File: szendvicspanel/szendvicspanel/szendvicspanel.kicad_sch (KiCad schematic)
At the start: 0 parts

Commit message: ANALOG_IN a mikrokontrolleres modulra is
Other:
- sheet Mikrovezérlő + PWM ports: added ANALOG_IN; removed none
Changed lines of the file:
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@@
+			)
+		)
+		(pin "ANALOG_IN" input
+			(at 121.92 156.21 180)
+			(effects
+				(font
+					(size 1.27 1.27)
+				)
+				(justify left)
 			)
 		)

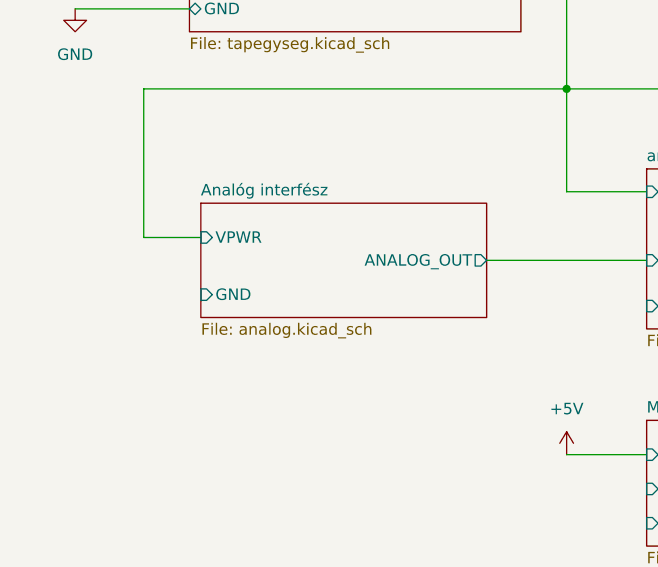
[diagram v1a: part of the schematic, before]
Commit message: KiCAD analóg interfész
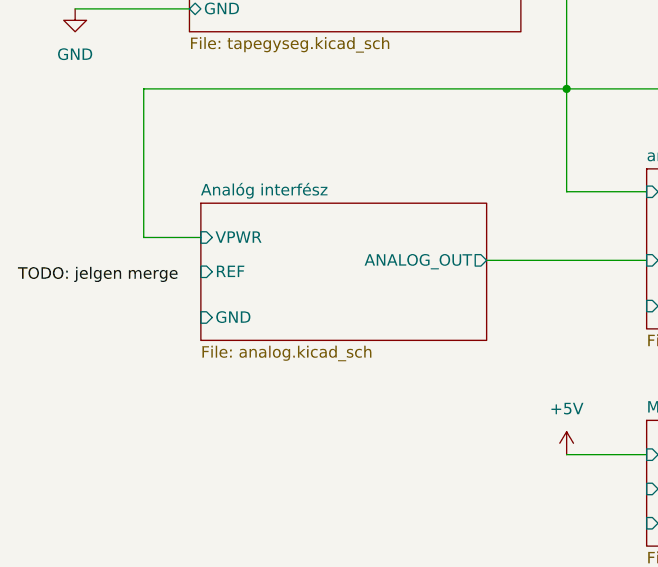
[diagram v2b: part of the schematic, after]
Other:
- sheet Analóg interfész ports: added REF; removed none
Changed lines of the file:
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@@
+		)
+	)
+	(label "TODO: jelgen merge"
+		(at 52.07 133.35 0)
+		(effects
+			(font
+				(size 1.27 1.27)
+			)
+			(justify left bottom)
 		)
 	)
@@
 	(sheet
 		(at 72.39 124.46)
-		(size 31.75 12.7)
+		(size 31.75 15.24)
 		(exclude_from_sim no)
 		(in_bom yes)
@@
 		)
 		(property "Sheetfile" "analog.kicad_sch"
-			(at 72.39 137.7446 0)
+			(at 72.39 140.2846 0)
 			(effects
 				(font
@@
 		)
 		(pin "GND" input
-			(at 72.39 134.62 180)
+			(at 72.39 137.16 180)
 			(effects
 				(font
@@
 			(effects
 				(font
+					(size 1.27 1.27)
+				)
+				(justify left)
+			)
+		)
+		(pin "REF" input
+			(at 72.39 132.08 180)
+			(effects
+				(font

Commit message: Analóg jelgen schematic copy+paste, output busz, analóg interfész pinjeinek frissítése
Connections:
- no-connect marks 0 -> 2
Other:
- sheet Analóg interfész ports: added +5V_IN, +5V_OUT, GND_IN, GND_OUT, REF_IN, VPWR_IN, VPWR_OUT, X; removed GND, REF, VPWR
- sheet analóg jelgen + PWM ports: added +5V, GND_IN, OUT{VPWR[1..8] GND[1..8] PWM[1..8]}, VPWR_IN; removed GND, PWM, SQR, TRI, VPWR
- note added: "Maximum 8 darab H-híd lehet"
- note removed: "TODO: 8 féle PWM 8 külön H-hídnak"

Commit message: Dokumentáció, Bandpass WIP
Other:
- sheet Analóg interfész ports: added none; removed REF_IN
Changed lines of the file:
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@@
-			)
-		)
-		(pin "REF_IN" input
-			(at 87.63 138.43 270)
-			(effects
-				(font
-					(size 1.27 1.27)
-				)
-				(justify left)
 			)
 		)

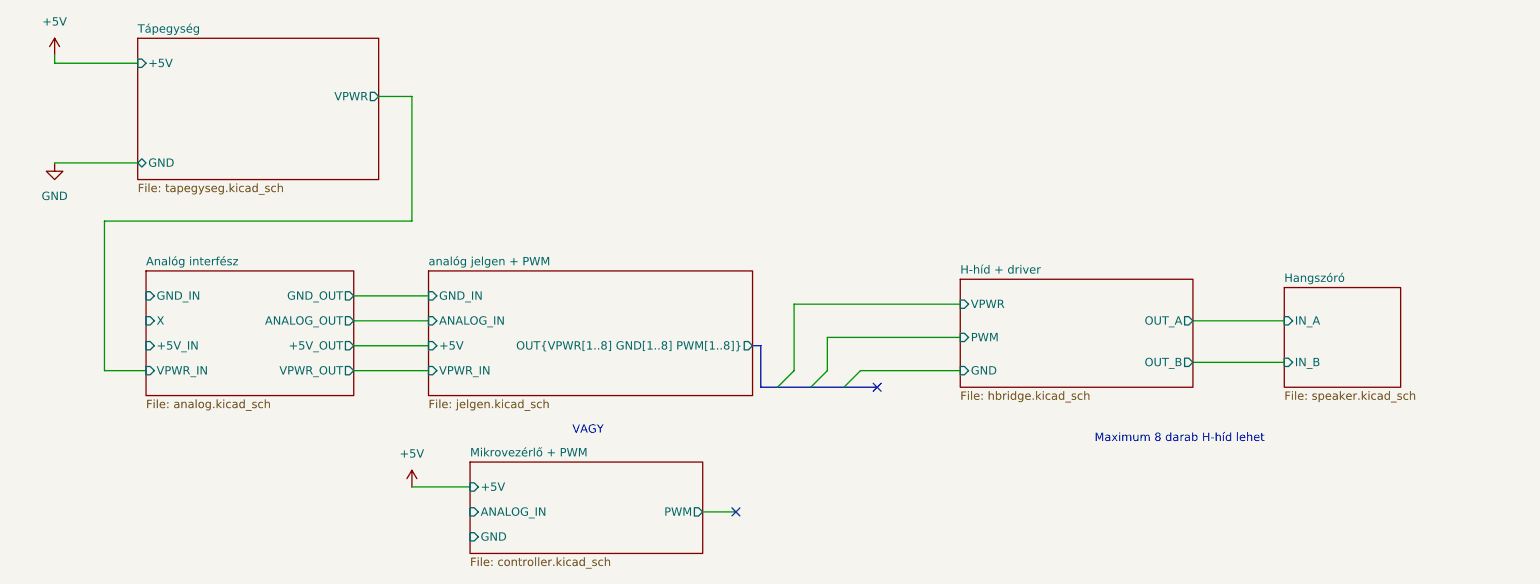
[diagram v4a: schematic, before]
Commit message: Átstrukturálás hierarchikus PCB-hez
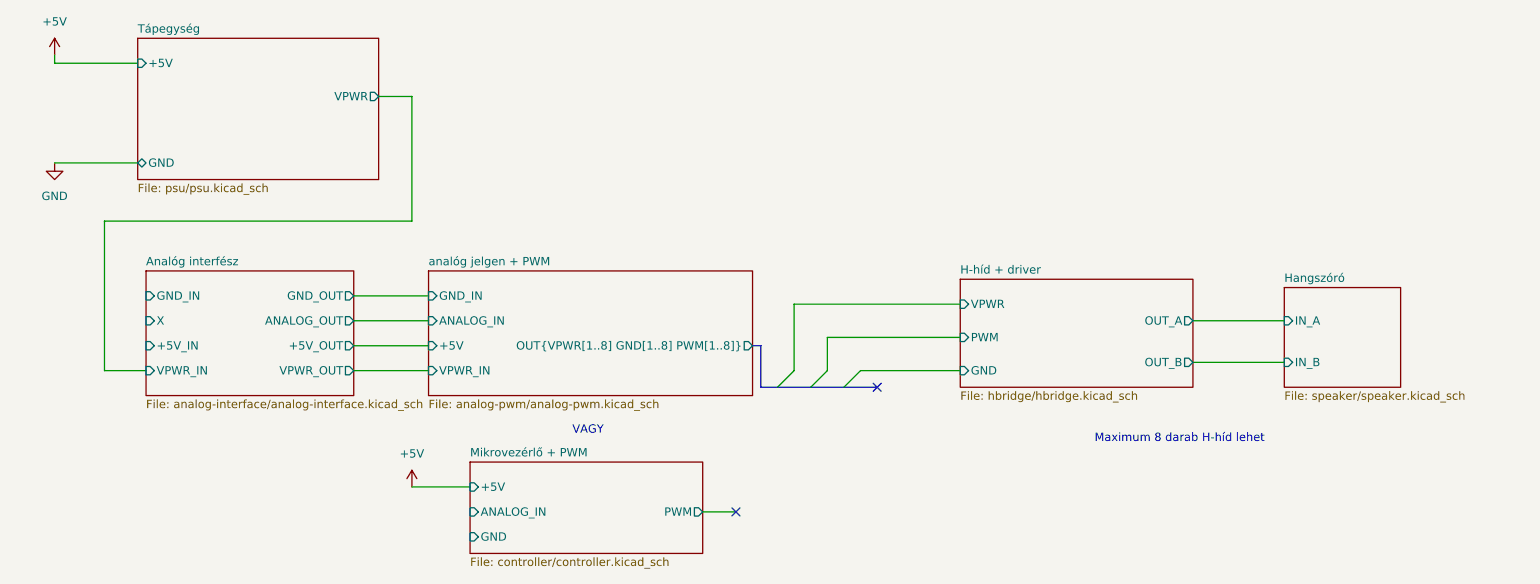
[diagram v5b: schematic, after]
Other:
- sheet Analóg interfész: file analog.kicad_sch -> analog-interface/analog-interface.kicad_sch
- sheet H-híd + driver: file hbridge.kicad_sch -> hbridge/hbridge.kicad_sch
- sheet Hangszóró: file speaker.kicad_sch -> speaker/speaker.kicad_sch
- sheet Mikrovezérlő + PWM: file controller.kicad_sch -> controller/controller.kicad_sch
- sheet Tápegység: file tapegyseg.kicad_sch -> psu/psu.kicad_sch
- sheet analóg jelgen + PWM: file jelgen.kicad_sch -> analog-pwm/analog-pwm.kicad_sch
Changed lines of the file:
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@@
 		(dnp no)
 		(fields_autoplaced yes)
-		(property "Reference" "#PWR01"
+		(property "Reference" "#PWR02"
 			(at 58.42 109.22 0)
 			(effects
@@
 			(project ""
 				(path "/2e536be4-7a69-4064-ab31-c73232c2dcfe"
-					(reference "#PWR01")
+					(reference "#PWR02")
 					(unit 1)
 				)
@@
 		(dnp no)
 		(fields_autoplaced yes)
-		(property "Reference" "#PWR02"
+		(property "Reference" "#PWR01"
 			(at 58.42 90.17 0)
 			(effects
@@
 			(project ""
 				(path "/2e536be4-7a69-4064-ab31-c73232c2dcfe"
-					(reference "#PWR02")
+					(reference "#PWR01")
 					(unit 1)
 				)
@@
 			)
 		)
-		(property "Sheetfile" "jelgen.kicad_sch"
+		(property "Sheetfile" "analog-pwm/analog-pwm.kicad_sch"
 			(at 115.57 139.0146 0)
 			(effects
@@
 			)
 		)
-		(property "Sheetfile" "speaker.kicad_sch"
+		(property "Sheetfile" "speaker/speaker.kicad_sch"
 			(at 246.38 137.7446 0)
 			(effects
@@
 			)
 		)
-		(property "Sheetfile" "analog.kicad_sch"
+		(property "Sheetfile" "analog-interface/analog-interface.kicad_sch"
 			(at 72.39 139.0146 0)
 			(effects
@@
 			)
 		)
-		(property "Sheetfile" "controller.kicad_sch"
+		(property "Sheetfile" "controller/controller.kicad_sch"
 			(at 121.92 163.1446 0)
 			(effects
@@
 			)
 		)
-		(property "Sheetfile" "hbridge.kicad_sch"
+		(property "Sheetfile" "hbridge/hbridge.kicad_sch"
 			(at 196.85 137.7446 0)
 			(effects
@@
 			)
 		)
-		(property "Sheetfile" "tapegyseg.kicad_sch"
+		(property "Sheetfile" "psu/psu.kicad_sch"
 			(at 71.12 105.9946 0)
 			(effects
